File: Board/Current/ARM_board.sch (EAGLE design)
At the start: 172 parts, among them IC3 STM32F437VI, IC4 LM358DT, J1 USART/I2C, J10 ANALOG, J11 DGND, J12 DPWR, J13 DIGITAL, J14 SGND, J15 SPWR, J16 SERVO, J2 I2C2/USART3, J3 USART2, J5 SPI, J6 Bluesmirf, J7 SWD, J8 AGND, J9 APWR, Q1 STL4P2UH7, Q2 2STR1230, SW1 SW, U1 LSM330DLC, U10 BAV99, U11 BAV99, U12 USBLC6-2, U13 USBLC6-2, U14 STMPS2171MTR, U15 MC74HC164, U17 DUAL-MOSFET, U19 DUAL-MOSFET, U3 NC7SZU04, U4 L6206Q, U5 L6206Q, U6 SI7617, U7 SI7617, U8 SI7617, U9 SI7617, Y2 8MHz

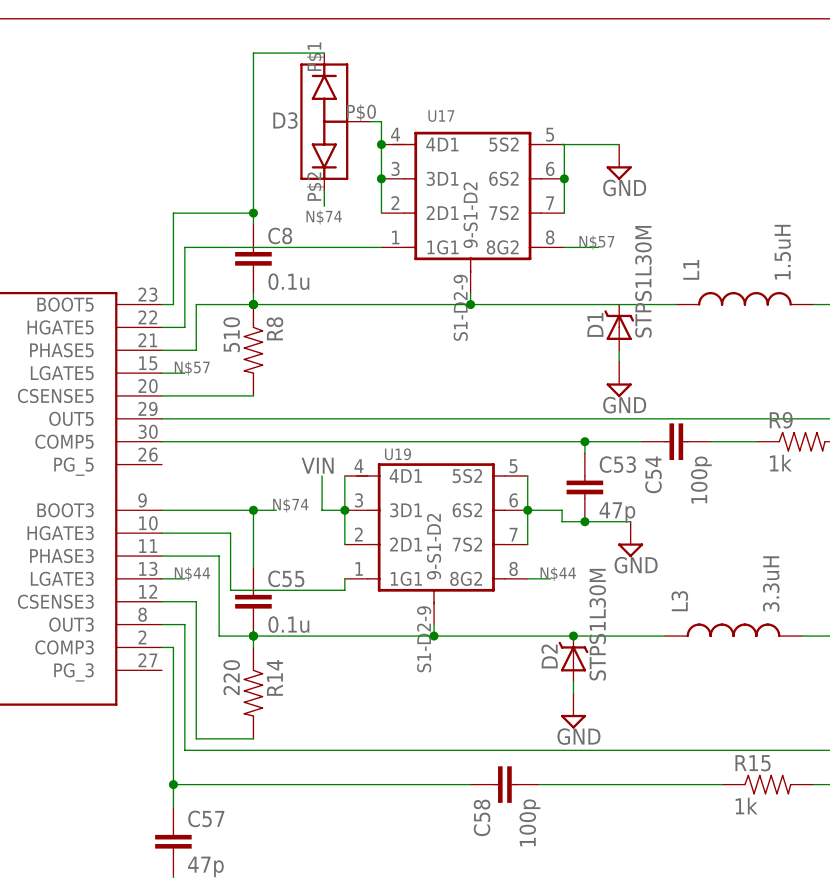
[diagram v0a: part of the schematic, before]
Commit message: Cleaned up Dual-Mosfet symbol on schematic
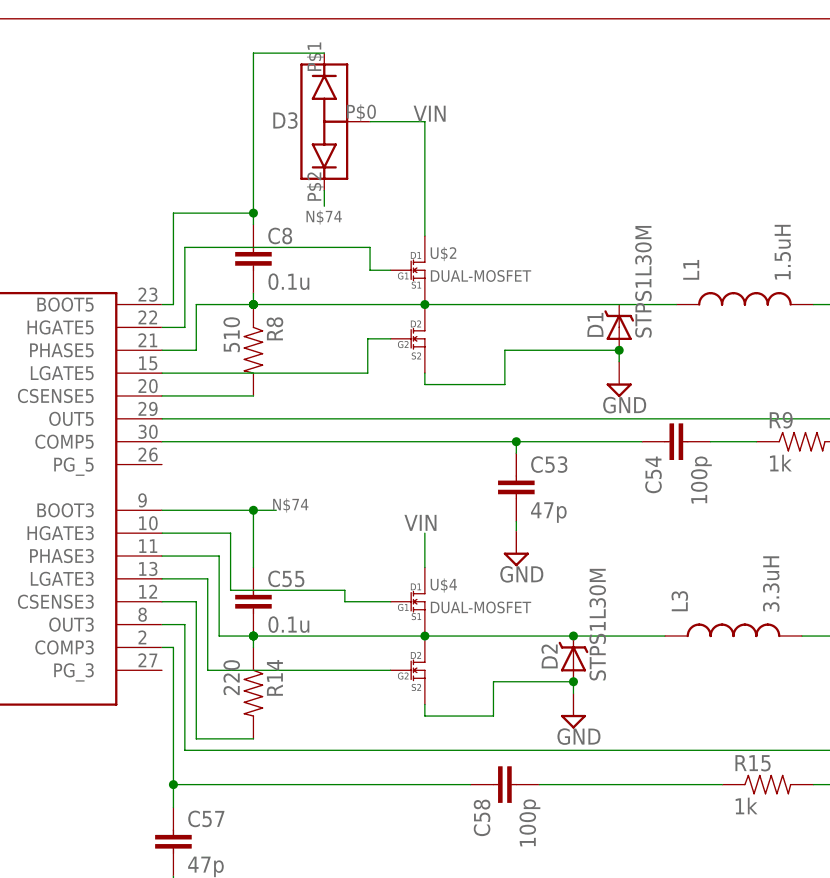
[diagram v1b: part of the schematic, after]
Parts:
- removed U17, U19: DUAL-MOSFET, r_cubed:DUAL-MOSFET
- added U$2, U$4: DUAL-MOSFET, r_cubed:DUAL-MOSFET
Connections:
- removed net N$32: U19.5S2, U19.6S2, U19.7S2
- removed net N$35: U17.5S2, U17.6S2, U17.7S2
- net GND: now also U$2.S2, U$4.S2
- net N$44: now also U$4.G2; no longer U19.8G2
- net N$56: now also U$2.G1; no longer U17.1G1
- net N$57: now also U$2.G2; no longer U17.8G2
- net N$66: now also U$2.S1; no longer U17.9-S1-D2
- net N$73: now also U$4.G1; no longer U19.1G1
- net N$75: now also U$4.S1; no longer U19.9-S1-D2
- net VIN: now also U$2.D1, U$4.D1; no longer U17.2D1, U17.3D1, U17.4D1, U19.2D1, U19.3D1, U19.4D1
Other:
- moved on the sheet: C53

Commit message: Cleaned out generated files from the current board directory. Finished laying out new regulator and all other schematic changes so far.
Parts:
- removed C33: 0.1u, SparkFun:CAP0402-CAP
- C26, C3, C4: device SparkFun:CAP0402-CAP -> SparkFun:CAP1206
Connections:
- net N$74 renamed BOOT3
- net 5V: no longer C33.1
- net GND: no longer C33.2
- net LDO5: now also D3.P$0
- net VIN: no longer D3.P$0

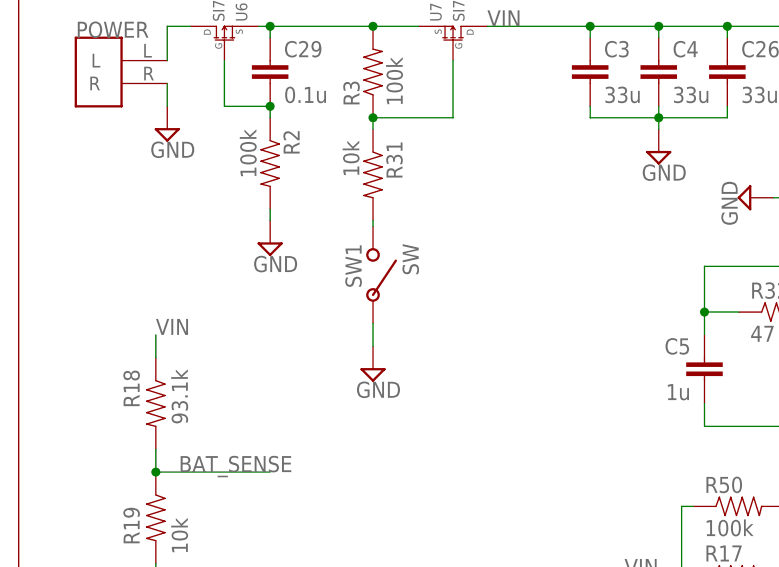
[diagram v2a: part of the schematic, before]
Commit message: Cleaned up bottom-left of the board. Moved the power LED above the switching section. Flipped the power switch around.
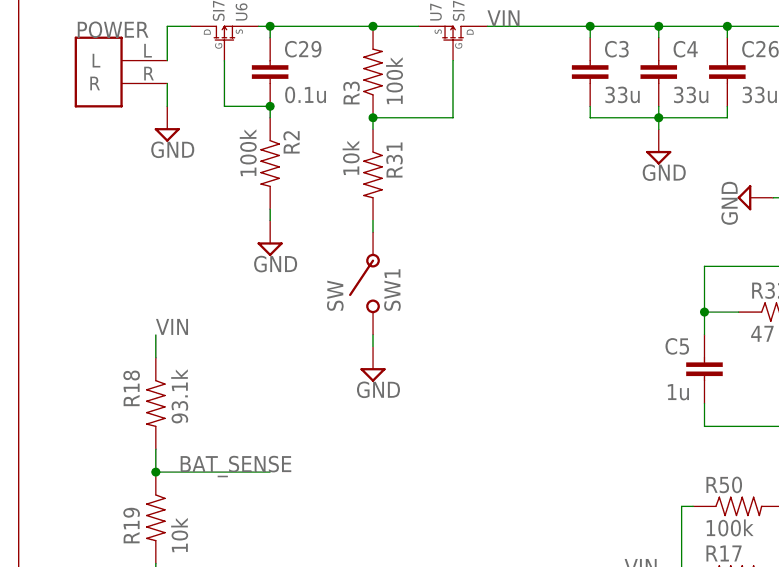
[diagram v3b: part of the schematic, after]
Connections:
- removed net N$22: R31.2, SW1.P$1
- new net N$10: R31.2, SW1.P$2
- net GND: now also SW1.P$1; no longer SW1.P$2
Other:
- moved on the sheet: SW1
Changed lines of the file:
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@@
 <grid distance="0.05" unitdist="inch" unit="inch" style="lines" multiple="1" display="no" altdistance="0.01" altunitdist="inch" altunit="inch"/>
 <layers>
-<layer number="1" name="Top" color="4" fill="1" visible="yes" active="no"/>
-<layer number="16" name="Bottom" color="1" fill="1" visible="yes" active="no"/>
-<layer number="17" name="Pads" color="2" fill="1" visible="yes" active="no"/>
-<layer number="18" name="Vias" color="2" fill="1" visible="yes" active="no"/>
-<layer number="19" name="Unrouted" color="6" fill="1" visible="yes" active="no"/>
-<layer number="20" name="Dimension" color="15" fill="1" visible="yes" active="no"/>
-<layer number="21" name="tPlace" color="15" fill="1" visible="yes" active="no"/>
-<layer number="22" name="bPlace" color="7" fill="1" visible="yes" active="no"/>
-<layer number="23" name="tOrigins" color="15" fill="1" visible="yes" active="no"/>
-<layer number="24" name="bOrigins" color="15" fill="1" visible="yes" active="no"/>
-<layer number="25" name="tNames" color="15" fill="1" visible="yes" active="no"/>
-<layer number="26" name="bNames" color="7" fill="1" visible="yes" active="no"/>
-<layer number="27" name="tValues" color="7" fill="1" visible="yes" active="no"/>
-<layer number="28" name="bValues" color="7" fill="1" visible="yes" active="no"/>
+<layer number="1" name="Top" color="4" fill="1" visible="no" active="no"/>
+<layer number="16" name="Bottom" color="1" fill="1" visible="no" active="no"/>
+<layer number="17" name="Pads" color="2" fill="1" visible="no" active="no"/>
+<layer number="18" name="Vias" color="2" fill="1" visible="no" active="no"/>
+<layer number="19" name="Unrouted" color="6" fill="1" visible="no" active="no"/>
+<layer number="20" name="Dimension" color="15" fill="1" visible="no" active="no"/>
+<layer number="21" name="tPlace" color="15" fill="1" visible="no" active="no"/>
+<layer number="22" name="bPlace" color="7" fill="1" visible="no" active="no"/>
+<layer number="23" name="tOrigins" color="15" fill="1" visible="no" active="no"/>
+<layer number="24" name="bOrigins" color="15" fill="1" visible="no" active="no"/>
+<layer number="25" name="tNames" color="15" fill="1" visible="no" active="no"/>
+<layer number="26" name="bNames" color="7" fill="1" visible="no" active="no"/>
+<layer number="27" name="tValues" color="7" fill="1" visible="no" active="no"/>
+<layer number="28" name="bValues" color="7" fill="1" visible="no" active="no"/>
 <layer number="29" name="tStop" color="7" fill="3" visible="no" active="no"/>
 <layer number="30" name="bStop" color="7" fill="6" visible="no" active="no"/>
@@
 <layer number="35" name="tGlue" color="7" fill="4" visible="no" active="no"/>
 <layer number="36" name="bGlue" color="7" fill="5" visible="no" active="no"/>
-<layer number="37" name="tTest" color="7" fill="1" visible="yes" active="no"/>
-<layer number="38" name="bTest" color="7" fill="1" visible="yes" active="no"/>
+<layer number="37" name="tTest" color="7" fill="1" visible="no" active="no"/>
+<layer number="38" name="bTest" color="7" fill="1" visible="no" active="no"/>
 <layer number="39" name="tKeepout" color="4" fill="11" visible="no" active="no"/>
 <layer number="40" name="bKeepout" color="1" fill="11" visible="no" active="no"/>
@@
 <layer number="44" name="Drills" color="7" fill="1" visible="no" active="no"/>
 <layer number="45" name="Holes" color="7" fill="1" visible="no" active="no"/>
-<layer number="46" name="Milling" color="3" fill="1" visible="yes" active="no"/>
-<layer number="47" name="Measures" color="7" fill="1" visible="yes" active="no"/>
-<layer number="48" name="Document" color="12" fill="1" visible="yes" active="no"/>
-<layer number="49" name="Reference" color="7" fill="1" visible="yes" active="no"/>
-<layer number="50" name="dxf" color="7" fill="1" visible="yes" active="no"/>
-<layer number="51" name="tDocu" color="7" fill="1" visible="yes" active="no"/>
-<layer number="52" name="bDocu" color="7" fill="1" visible="yes" active="no"/>
-<layer number="53" name="tGND_GNDA" color="7" fill="9" visible="yes" active="no"/>
-<layer number="54" name="bGND_GNDA" color="1" fill="9" visible="yes" active="no"/>
-<layer number="56" name="wert" color="7" fill="1" visible="yes" active="no"/>
+<layer number="46" name="Milling" color="3" fill="1" visible="no" active="no"/>
+<layer number="47" name="Measures" color="7" fill="1" visible="no" active="no"/>
+<layer number="48" name="Document" color="12" fill="1" visible="no" active="no"/>
+<layer number="49" name="Reference" color="7" fill="1" visible="no" active="no"/>
+<layer number="50" name="dxf" color="7" fill="1" visible="no" active="no"/>
+<layer number="51" name="tDocu" color="7" fill="1" visible="no" active="no"/>
+<layer number="52" name="bDocu" color="7" fill="1" visible="no" active="no"/>
+<layer number="53" name="tGND_GNDA" color="7" fill="9" visible="no" active="no"/>
+<layer number="54" name="bGND_GNDA" color="1" fill="9" visible="no" active="no"/>
+<layer number="56" name="wert" color="7" fill="1" visible="no" active="no"/>
 <layer number="91" name="Nets" color="2" fill="1" visible="yes" active="yes"/>
 <layer number="92" name="Busses" color="1" fill="1" visible="yes" active="yes"/>
@@
 <instance part="R39" gate="G$1" x="335.28" y="21.59"/>
 <instance part="R1" gate="G$1" x="356.87" y="116.84" rot="R180"/>
-<instance part="SW1" gate="G$1" x="39.37" y="274.32" rot="MR180"/>
+<instance part="SW1" gate="G$1" x="39.37" y="274.32" rot="MR0"/>
 <instance part="SERVO_PWR" gate="G$1" x="13.335" y="220.345"/>
 <instance part="POWER" gate="G$1" x="6.35" y="295.91"/>
@@
 </segment>
 <segment>
-<pinref part="SW1" gate="G$1" pin="P$2"/>
-<pinref part="SUPPLY43" gate="GND" pin="GND"/>
-<wire x1="39.37" y1="269.24" x2="39.37" y2="266.7" width="0.1524" layer="91"/>
-</segment>
-<segment>
 <pinref part="R42" gate="G$1" pin="1"/>
 <pinref part="SUPPLY44" gate="GND" pin="GND"/>
@@
 <wire x1="341.63" y1="62.23" x2="341.63" y2="60.96" width="0.1524" layer="91"/>
 </segment>
+<segment>
+<pinref part="SW1" gate="G$1" pin="P$1"/>
+<pinref part="SUPPLY43" gate="GND" pin="GND"/>
+<wire x1="39.37" y1="267.97" x2="39.37" y2="266.7" width="0.1524" layer="91"/>
+</segment>
 </net>
 <net name="5V" class="0">
@@
 </segment>
 </net>
-<net name="N$22" class="0">
-<segment>
-<pinref part="R31" gate="G$1" pin="2"/>
-<pinref part="SW1" gate="G$1" pin="P$1"/>
-<wire x1="39.37" y1="280.67" x2="39.37" y2="280.035" width="0.1524" layer="91"/>
-</segment>
-</net>
 <net name="DIGITAL14" class="0">
 <segment>
@@
 </segment>
 </net>
+<net name="N$10" class="0">
+<segment>
+<pinref part="R31" gate="G$1" pin="2"/>
+<pinref part="SW1" gate="G$1" pin="P$2"/>
+<wire x1="39.37" y1="280.67" x2="39.37" y2="279.4" width="0.1524" layer="91"/>
+</segment>
+</net>

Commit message: More work on the schematic / layout.
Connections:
- net +3V3: now also SD.SHIELD@2
- net BOOT1: now also SD.SHIELD@4
- net GND: no longer SD.SHIELD@2, SD.SHIELD@4
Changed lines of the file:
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@@
 <part name="U$2" library="r_cubed" deviceset="DUAL-MOSFET" device=""/>
 <part name="U$4" library="r_cubed" deviceset="DUAL-MOSFET" device=""/>
+<part name="+3V12" library="supply1" deviceset="+3V3" device=""/>
 </parts>
 <sheets>
@@
 <instance part="U$2" gate="G$1" x="170.18" y="276.86"/>
 <instance part="U$4" gate="G$1" x="170.18" y="240.03"/>
+<instance part="+3V12" gate="G$1" x="350.52" y="73.66" smashed="yes">
+<attribute name="VALUE" x="347.98" y="71.12" size="1.778" layer="96" rot="R90"/>
+</instance>
 </instances>
 <busses>
@@
 <pinref part="SD" gate="G$1" pin="SHIELD@3"/>
 <wire x1="363.22" y1="64.77" x2="359.41" y2="64.77" width="0.1524" layer="91"/>
-<wire x1="359.41" y1="64.77" x2="359.41" y2="67.31" width="0.1524" layer="91"/>
 <pinref part="SD" gate="G$1" pin="SHIELD@1"/>
-<wire x1="359.41" y1="67.31" x2="359.41" y2="69.85" width="0.1524" layer="91"/>
+<wire x1="359.41" y1="64.77" x2="359.41" y2="69.85" width="0.1524" layer="91"/>
 <wire x1="359.41" y1="69.85" x2="363.22" y2="69.85" width="0.1524" layer="91"/>
 <wire x1="359.41" y1="69.85" x2="359.41" y2="80.01" width="0.1524" layer="91"/>
@@
 <junction x="359.41" y="69.85"/>
 <pinref part="SUPPLY30" gate="GND" pin="GND"/>
-<wire x1="359.41" y1="64.77" x2="359.41" y2="62.23" width="0.1524" layer="91"/>
+<wire x1="359.41" y1="64.77" x2="359.41" y2="60.96" width="0.1524" layer="91"/>
 <junction x="359.41" y="64.77"/>
-<pinref part="SD" gate="G$1" pin="SHIELD@2"/>
-<wire x1="359.41" y1="62.23" x2="359.41" y2="60.96" width="0.1524" layer="91"/>
-<wire x1="363.22" y1="67.31" x2="359.41" y2="67.31" width="0.1524" layer="91"/>
-<pinref part="SD" gate="G$1" pin="SHIELD@4"/>
-<wire x1="363.22" y1="62.23" x2="359.41" y2="62.23" width="0.1524" layer="91"/>
-<junction x="359.41" y="67.31"/>
-<junction x="359.41" y="62.23"/>
 </segment>
 <segment>
@@
 <wire x1="341.63" y1="71.12" x2="341.63" y2="69.85" width="0.1524" layer="91"/>
 </segment>
+<segment>
+<pinref part="SD" gate="G$1" pin="SHIELD@2"/>
+<wire x1="363.22" y1="67.31" x2="350.52" y2="67.31" width="0.1524" layer="91"/>
+<pinref part="+3V12" gate="G$1" pin="+3V3"/>
+<wire x1="350.52" y1="71.12" x2="350.52" y2="67.31" width="0.1524" layer="91"/>
+</segment>
 </net>
 <net name="N$47" class="0">
@@
 <label x="194.31" y="144.78" size="1.778" layer="95"/>
 </segment>
+<segment>
+<pinref part="SD" gate="G$1" pin="SHIELD@4"/>
+<wire x1="363.22" y1="62.23" x2="350.52" y2="62.23" width="0.1524" layer="91"/>
+<label x="350.52" y="62.23" size="1.778" layer="95"/>
+</segment>
 </net>
